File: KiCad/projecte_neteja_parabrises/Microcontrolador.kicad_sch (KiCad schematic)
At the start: 14 parts, among them J1 Conn_01x05_Pin, SW1 SW_Omron_B3FS, U3 HDC2080, Y1 Crystal

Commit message: Pines
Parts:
- renumbered C4 to C17, C5 to C3, C6 to C4, R1 to R10, R3 to R7, R2 to R9, SW1 to SW4, U3 to U6
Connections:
- net GATE B2: now reaches 11.26 (RC1)
- no-connect marks 16 -> 15
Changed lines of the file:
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@@
 	)
 	(no_connect
-		(at 34.29 73.66)
-	)
-	(no_connect
 		(at 83.82 119.38)
 	)
@@
 	(wire
 		(pts
+			(xy 30.734 73.66) (xy 34.29 73.66)
+		)
+		(stroke
+			(width 0)
+			(type default)
+		)
+	)
+	(wire
+		(pts
 			(xy 105.41 104.14) (xy 108.204 104.14)
 		)
@@
 		)
 	)
+	(global_label "GATE B2"
+		(shape input)
+		(at 30.734 73.66 180)
+		(fields_autoplaced yes)
+		(effects
+			(font
+				(size 1.27 1.27)
+			)
+			(justify right)
+		)
+		(property "Intersheetrefs" "${INTERSHEET_REFS}"
+			(at 19.8265 73.66 0)
+			(effects
+				(font
+					(size 1.27 1.27)
+				)
+				(justify right)
+				(hide yes)
+			)
+		)
+	)
 	(global_label "SCL"
 		(shape input)
@@
 		(dnp no)
 		(fields_autoplaced yes)
-		(property "Reference" "R2"
+		(property "Reference" "R9"
 			(at 254.635 26.6699 0)
 			(effects
@@
 		(dnp no)
 		(fields_autoplaced yes)
-		(property "Reference" "#PWR015"
+		(property "Reference" "#PWR037"
 			(at 34.544 38.608 0)
 			(effects
@@
 		(on_board yes)
 		(dnp no)
-		(property "Reference" "#PWR012"
+		(property "Reference" "#PWR0110"
 			(at 76.2 40.64 0)
 			(effects
@@
 		(dnp no)
 		(fields_autoplaced yes)
-		(property "Reference" "U3"
+		(property "Reference" "U6"
 			(at 236.4583 30.48 0)
 			(effects
@@
 		(on_board yes)
 		(dnp no)
-		(property "Reference" "11"
+		(property "Reference" "U?"
 			(at 68.072 87.376 0)
 			(effects
@@
 				)
 			)
+			(project "projecte_neteja_parabrises"
+				(path "/83fe8808-b70b-463e-9fcd-89556c9690a9/7b0ed2a6-dd0e-4fb8-9a3e-b81f5336277e"
+					(reference "U?")
+					(unit 1)
+				)
+			)
 		)
 	)
@@
 		(dnp no)
 		(fields_autoplaced yes)
-		(property "Reference" "C6"
+		(property "Reference" "C4"
 			(at 171.45 44.4499 0)
 			(effects
@@
 		(dnp no)
 		(fields_autoplaced yes)
-		(property "Reference" "SW1"
+		(property "Reference" "SW4"
 			(at 61.214 16.002 0)
 			(effects
@@
 		(dnp no)
 		(fields_autoplaced yes)
-		(property "Reference" "#PWR02"
+		(property "Reference" "#PWR022"
 			(at 153.035 55.88 0)
 			(effects
@@
 		(on_board yes)
 		(dnp no)
-		(property "Reference" "#PWR05"
+		(property "Reference" "#PWR?"
 			(at 81.28 39.624 0)
 			(effects
@@
 				)
 			)
+			(project "projecte_neteja_parabrises"
+				(path "/83fe8808-b70b-463e-9fcd-89556c9690a9/7b0ed2a6-dd0e-4fb8-9a3e-b81f5336277e"
+					(reference "#PWR?")
+					(unit 1)
+				)
+			)
 		)
 	)
@@
 		(dnp no)
 		(fields_autoplaced yes)
-		(property "Reference" "#PWR07"
+		(property "Reference" "#PWR036"
 			(at 70.739 29.972 0)
 			(effects
@@
 		(on_board yes)
 		(dnp no)
-		(property "Reference" "#PWR03"
+		(property "Reference" "#PWR?"
 			(at 23.622 95.758 0)
 			(effects
@@
 				)
 			)
+			(project "projecte_neteja_parabrises"
+				(path "/83fe8808-b70b-463e-9fcd-89556c9690a9/7b0ed2a6-dd0e-4fb8-9a3e-b81f5336277e"
+					(reference "#PWR?")
+					(unit 1)
+				)
+			)
 		)
 	)
@@
 		(dnp no)
 		(fields_autoplaced yes)
-		(property "Reference" "C5"
+		(property "Reference" "C3"
 			(at 156.21 44.4499 0)
 			(effects
@@
 		(on_board yes)
 		(dnp no)
-		(property "Reference" "#PWR06"
+		(property "Reference" "#PWR024"
 			(at 222.25 49.53 0)
 			(effects
@@
 		(on_board yes)
 		(dnp no)
-		(property "Reference" "C4"
+		(property "Reference" "C17"
 			(at 115.57 76.2 90)
 			(effects
@@
 		(dnp no)
 		(fields_autoplaced yes)
-		(property "Reference" "#PWR08"
+		(property "Reference" "#PWR09"
 			(at 106.68 90.17 0)
 			(effects
@@
 		(dnp no)
 		(fields_autoplaced yes)
-		(property "Reference" "#PWR014"
+		(property "Reference" "#PWR0112"
 			(at 119.888 85.09 0)
 			(effects
@@
 		(dnp no)
 		(fields_autoplaced yes)
-		(property "Reference" "#PWR04"
+		(property "Reference" "#PWR025"
 			(at 234.315 59.69 0)
 			(effects
@@
 		(on_board yes)
 		(dnp no)
-		(property "Reference" "R1"
+		(property "Reference" "R10"
 			(at 261.239 49.5301 0)
 			(effects
@@
 		(dnp no)
 		(fields_autoplaced yes)
-		(property "Reference" "#PWR01"
+		(property "Reference" "#PWR023"
 			(at 168.275 55.88 0)
 			(effects
@@
 		(on_board yes)
 		(dnp no)
-		(property "Reference" "C2"
+		(property "Reference" "C?"
 			(at 33.655 87.63 90)
 			(effects
@@
 				)
 			)
+			(project "projecte_neteja_parabrises"
+				(path "/83fe8808-b70b-463e-9fcd-89556c9690a9/7b0ed2a6-dd0e-4fb8-9a3e-b81f5336277e"
+					(reference "C?")
+					(unit 1)
+				)
+			)
 		)
 	)
@@
 		(dnp no)
 		(fields_autoplaced yes)
-		(property "Reference" "R3"
+		(property "Reference" "R7"
 			(at 52.324 17.272 90)
 			(effects

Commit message: huella
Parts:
- U4: renamed from 11; footprint (none) -> Package_DFN_QFN:QFN-44-1EP_7x7mm_P0.5mm_EP5.2x5.2mm
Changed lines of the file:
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@@
 		(on_board yes)
 		(dnp no)
-		(property "Reference" "U?"
+		(property "Reference" "U4"
 			(at 68.072 87.376 0)
 			(effects
@@
 			)
 		)
-		(property "Footprint" ""
+		(property "Footprint" "Package_DFN_QFN:QFN-44-1EP_7x7mm_P0.5mm_EP5.2x5.2mm"
 			(at 132.334 68.326 0)
 			(effects
@@
 			(project "projecte_neteja_parabrises"
 				(path "/83fe8808-b70b-463e-9fcd-89556c9690a9/7b0ed2a6-dd0e-4fb8-9a3e-b81f5336277e"
-					(reference "U?")
+					(reference "U4")
 					(unit 1)
 				)
@@
 		(on_board yes)
 		(dnp no)
-		(property "Reference" "#PWR?"
+		(property "Reference" "#PWR0101"
 			(at 81.28 39.624 0)
 			(effects
@@
 			(project "projecte_neteja_parabrises"
 				(path "/83fe8808-b70b-463e-9fcd-89556c9690a9/7b0ed2a6-dd0e-4fb8-9a3e-b81f5336277e"
-					(reference "#PWR?")
+					(reference "#PWR0101")
 					(unit 1)
 				)
@@
 		(on_board yes)
 		(dnp no)
-		(property "Reference" "#PWR?"
+		(property "Reference" "#PWR0102"
 			(at 23.622 95.758 0)
 			(effects
@@
 			(project "projecte_neteja_parabrises"
 				(path "/83fe8808-b70b-463e-9fcd-89556c9690a9/7b0ed2a6-dd0e-4fb8-9a3e-b81f5336277e"
-					(reference "#PWR?")
+					(reference "#PWR0102")
 					(unit 1)
 				)
@@
 		(on_board yes)
 		(dnp no)
-		(property "Reference" "C?"
+		(property "Reference" "C2"
 			(at 33.655 87.63 90)
 			(effects
@@
 			(project "projecte_neteja_parabrises"
 				(path "/83fe8808-b70b-463e-9fcd-89556c9690a9/7b0ed2a6-dd0e-4fb8-9a3e-b81f5336277e"
-					(reference "C?")
-					(unit 1)
-				)
+					(reference "C2")
+					(unit 1)
+				)

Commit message: pcb placement
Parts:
- Y1: footprint Crystal:Crystal_SMD_HC49-SD -> Crystal:Crystal_SMD_EuroQuartz_EQ161-2Pin_3.2x1.5mm_HandSoldering
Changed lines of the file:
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@@
 			)
 		)
-		(property "Footprint" "Crystal:Crystal_SMD_HC49-SD"
+		(property "Footprint" "Crystal:Crystal_SMD_EuroQuartz_EQ161-2Pin_3.2x1.5mm_HandSoldering"
 			(at 160.655 39.37 0)
 			(effects

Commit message: pcb
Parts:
- removed SW4: SW_Omron_B3FS, Button_Switch_SMD:SW_SPST_Omron_B3FS-100xP, symbol Switch:SW_Omron_B3FS
- added SW3: CALEFACTOR, Button_Switch_SMD:SW_Push_SPST_NO_Alps_SKRK, symbol Switch:SW_Push
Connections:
- net CANRX: now also U4.25 (RC0); no longer U4.36 (RP19)
- net CANTX: now also U4.26 (RC1); no longer U4.37 (RP20)
- net FC1: now also U4.4 (RC8); no longer U4.32 (RA8)
- net FC2: now also U4.3 (RC7); no longer U4.33 (RB4)
- net GATE B: now also U4.20 (RA1); no longer U4.25 (RC0)
- net GATE B2: now also U4.19 (RA0); no longer U4.26 (RC1)
- net GATE C: now also U4.14 (RB14); no longer U4.27 (RC2)
- net GND: now also SW3.2
- net SW1: now also U4.35 (RA9); no longer U4.2 (RC6)
- net SW2: now also U4.36 (RP19); no longer U4.3 (RC7)
- net SW3: now also U4.37 (RP20); no longer U4.4 (RC8)
- net SWB: now also U4.42 (RB6); no longer U4.20 (RA1)
- net SWC: now also U4.41 (RB5); no longer U4.19 (RA0)
- net at R7.2: now also SW3.1

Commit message: pcb
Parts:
- SW3: value CALEFACTOR -> SW
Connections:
- net GATE B2: now also U4.14 (RB14); no longer U4.19 (RA0)
- net GATE C: now also U4.13 (RA7); no longer U4.14 (RB14)
- net RX: now also U4.24 (RP3); no longer U4.23 (RP2)
- net TX: now also U4.23 (RP2); no longer U4.24 (RP3)
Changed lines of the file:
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@@
 	)
 	(no_connect
-		(at 88.9 48.26)
+		(at 59.69 45.72)
 	)
 	(no_connect
@@
 	(global_label "RX"
 		(shape input)
-		(at 29.718 58.42 180)
+		(at 29.21 63.5 180)
 		(fields_autoplaced yes)
 		(effects
@@
 		)
 		(property "Intersheetrefs" "${INTERSHEET_REFS}"
-			(at 24.2533 58.42 0)
+			(at 23.7453 63.5 0)
 			(effects
 				(font
@@
 	(global_label "GATE C"
 		(shape input)
-		(at 83.82 48.26 90)
-		(fields_autoplaced yes)
-		(effects
-			(font
-				(size 1.27 1.27)
-			)
-			(justify left)
-		)
-		(property "Intersheetrefs" "${INTERSHEET_REFS}"
-			(at 83.82 38.562 90)
+		(at 88.9 48.26 90)
+		(fields_autoplaced yes)
+		(effects
+			(font
+				(size 1.27 1.27)
+			)
+			(justify left)
+		)
+		(property "Intersheetrefs" "${INTERSHEET_REFS}"
+			(at 88.9 38.562 90)
 			(effects
 				(font
@@
 	(global_label "GATE B2"
 		(shape input)
-		(at 59.69 45.72 90)
-		(fields_autoplaced yes)
-		(effects
-			(font
-				(size 1.27 1.27)
-			)
-			(justify left)
-		)
-		(property "Intersheetrefs" "${INTERSHEET_REFS}"
-			(at 59.69 34.8125 90)
+		(at 83.82 48.26 90)
+		(fields_autoplaced yes)
+		(effects
+			(font
+				(size 1.27 1.27)
+			)
+			(justify left)
+		)
+		(property "Intersheetrefs" "${INTERSHEET_REFS}"
+			(at 83.82 37.3525 90)
 			(effects
 				(font
@@
 	(global_label "TX"
 		(shape output)
-		(at 29.21 63.5 180)
+		(at 29.718 58.42 180)
 		(fields_autoplaced yes)
 		(effects
@@
 		)
 		(property "Intersheetrefs" "${INTERSHEET_REFS}"
-			(at 24.0477 63.5 0)
+			(at 24.5557 58.42 0)
 			(effects
 				(font
@@
 			)
 		)
-		(property "Value" "CALEFACTOR"
+		(property "Value" "SW"
 			(at 63.119 17.907 0)
 			(effects

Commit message: pcb
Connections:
- net FC1: now also U4.34 (RA4); no longer U4.4 (RC8)
- net FC2: now also U4.33 (RB4); no longer U4.3 (RC7)
- net SW1: now also U4.11 (RB13); no longer U4.35 (RA9)
- net SW2: now also U4.4 (RC8); no longer U4.36 (RP19)
- net SW3: now also U4.3 (RC7); no longer U4.37 (RP20)
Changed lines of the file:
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@@
+	)
+	(no_connect
+		(at 105.41 88.9)
 	)
 	(no_connect
@@
 	)
 	(no_connect
-		(at 31.242 109.22)
+		(at 48.26 119.38)
 	)
 	(no_connect
@@
 	)
 	(no_connect
-		(at 105.41 88.9)
+		(at 58.42 119.38)
 	)
 	(no_connect
-		(at 44.45 119.38)
-	)
-	(no_connect
-		(at 105.41 58.42)
+		(at 53.34 124.46)
 	)
 	(no_connect
@@
 	(wire
 		(pts
-			(xy 58.42 119.38) (xy 58.42 124.46)
-		)
-		(stroke
-			(width 0)
-			(type default)
-		)
-	)
-	(wire
-		(pts
 			(xy 39.37 27.432) (xy 39.37 28.702)
 		)
@@
 	(wire
 		(pts
-			(xy 31.242 109.22) (xy 34.29 109.22)
-		)
-		(stroke
-			(width 0)
-			(type default)
-		)
-	)
-	(wire
-		(pts
 			(xy 29.718 58.42) (xy 34.29 58.42)
 		)
@@
 	(global_label "FC1"
 		(shape input)
-		(at 109.22 93.98 0)
-		(fields_autoplaced yes)
-		(effects
-			(font
-				(size 1.27 1.27)
-			)
-			(justify left)
-		)
-		(property "Intersheetrefs" "${INTERSHEET_REFS}"
-			(at 115.7733 93.98 0)
-			(effects
-				(font
-					(size 1.27 1.27)
-				)
-				(justify left)
+		(at 44.45 119.38 270)
+		(fields_autoplaced yes)
+		(effects
+			(font
+				(size 1.27 1.27)
+			)
+			(justify right)
+		)
+		(property "Intersheetrefs" "${INTERSHEET_REFS}"
+			(at 44.45 125.9333 90)
+			(effects
+				(font
+					(size 1.27 1.27)
+				)
+				(justify right)
 				(hide yes)
 			)
@@
 	(global_label "SW3"
 		(shape input)
-		(at 58.42 124.46 270)
-		(fields_autoplaced yes)
-		(effects
-			(font
-				(size 1.27 1.27)
-			)
-			(justify right)
-		)
-		(property "Intersheetrefs" "${INTERSHEET_REFS}"
-			(at 58.42 131.3156 90)
-			(effects
-				(font
-					(size 1.27 1.27)
-				)
-				(justify right)
+		(at 108.458 99.06 0)
+		(fields_autoplaced yes)
+		(effects
+			(font
+				(size 1.27 1.27)
+			)
+			(justify left)
+		)
+		(property "Intersheetrefs" "${INTERSHEET_REFS}"
+			(at 115.3136 99.06 0)
+			(effects
+				(font
+					(size 1.27 1.27)
+				)
+				(justify left)
 				(hide yes)
 			)
@@
 	(global_label "SW1"
 		(shape input)
-		(at 48.26 119.38 270)
-		(fields_autoplaced yes)
-		(effects
-			(font
-				(size 1.27 1.27)
-			)
-			(justify right)
-		)
-		(property "Intersheetrefs" "${INTERSHEET_REFS}"
-			(at 48.26 126.2356 90)
-			(effects
-				(font
-					(size 1.27 1.27)
-				)
-				(justify right)
+		(at 105.41 58.42 0)
+		(fields_autoplaced yes)
+		(effects
+			(font
+				(size 1.27 1.27)
+			)
+			(justify left)
+		)
+		(property "Intersheetrefs" "${INTERSHEET_REFS}"
+			(at 112.2656 58.42 0)
+			(effects
+				(font
+					(size 1.27 1.27)
+				)
+				(justify left)
 				(hide yes)
 			)
@@
 	(global_label "FC2"
 		(shape input)
-		(at 108.458 99.06 0)
-		(fields_autoplaced yes)
-		(effects
-			(font
-				(size 1.27 1.27)
-			)
-			(justify left)
-		)
-		(property "Intersheetrefs" "${INTERSHEET_REFS}"
-			(at 115.0113 99.06 0)
-			(effects
-				(font
-					(size 1.27 1.27)
-				)
-				(justify left)
+		(at 34.29 109.22 180)
+		(fields_autoplaced yes)
+		(effects
+			(font
+				(size 1.27 1.27)
+			)
+			(justify right)
+		)
+		(property "Intersheetrefs" "${INTERSHEET_REFS}"
+			(at 27.7367 109.22 0)
+			(effects
+				(font
+					(size 1.27 1.27)
+				)
+				(justify right)
 				(hide yes)
 			)
@@
 	(global_label "SW2"
 		(shape input)
-		(at 53.34 124.46 270)
-		(fields_autoplaced yes)
-		(effects
-			(font
-				(size 1.27 1.27)
-			)
-			(justify right)
-		)
-		(property "Intersheetrefs" "${INTERSHEET_REFS}"
-			(at 53.34 131.3156 90)
-			(effects
-				(font
-					(size 1.27 1.27)
-				)
-				(justify right)
-				(hide yes)
-			)
+		(at 109.22 93.98 0)
+		(fields_autoplaced yes)
+		(effects
+			(font
+				(size 1.27 1.27)
+			)
+			(justify left)
+		)
+		(property "Intersheetrefs" "${INTERSHEET_REFS}"
+			(at 116.0756 93.98 0)
+			(effects
+				(font
+					(size 1.27 1.27)
+				)
+				(justify left)
+				(hide yes)
+			)

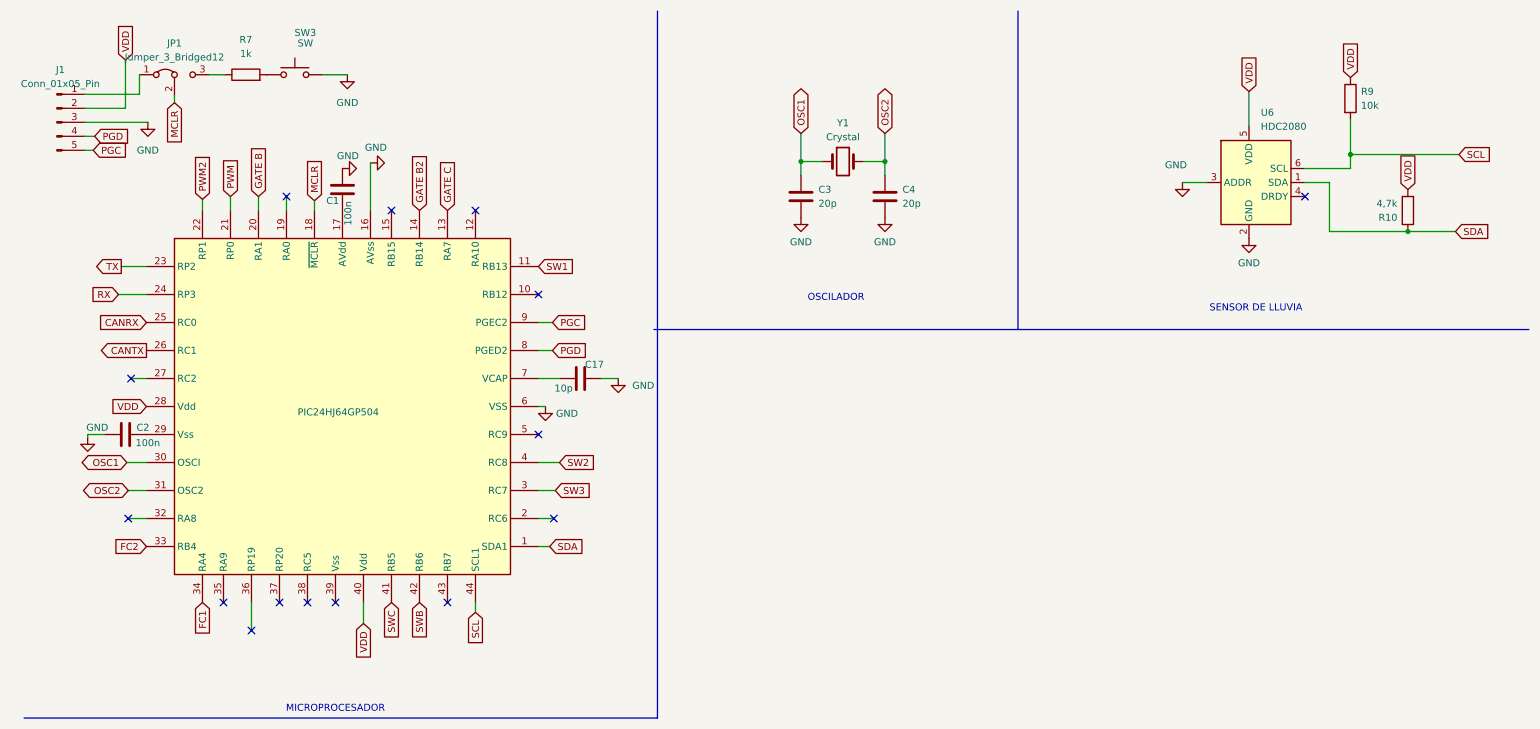
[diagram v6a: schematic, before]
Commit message: actualitzacio pcb
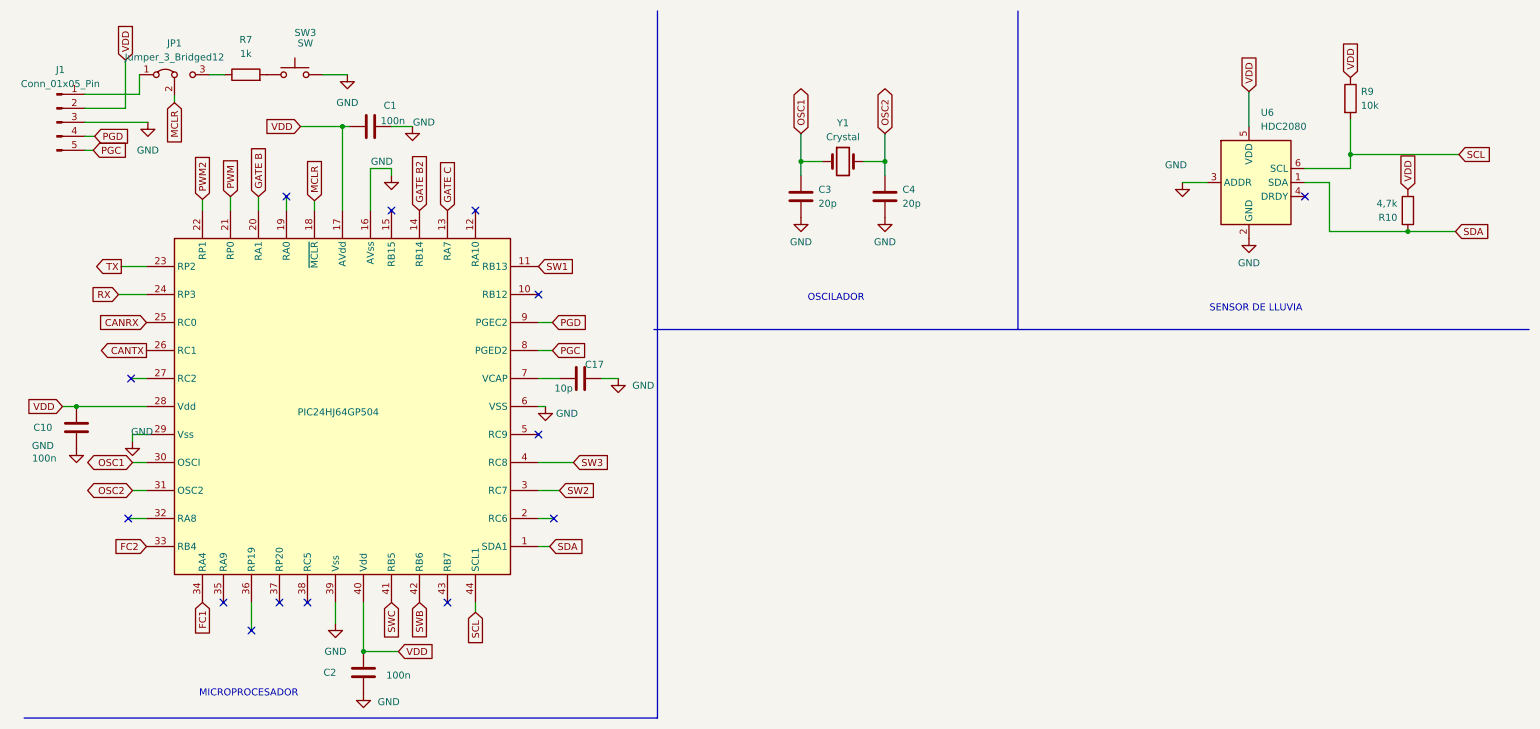
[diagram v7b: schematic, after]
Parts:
- added C10: 100n, Capacitor_SMD:C_0805_2012Metric, symbol Device:C
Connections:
- net GND: now also C1.1, U4.29 (Vss), U4.39 (Vss), C10.1; no longer C1.2
- net PGC: now also U4.8 (PGED2); no longer U4.9 (PGEC2)
- net PGD: now also U4.9 (PGEC2); no longer U4.8 (PGED2)
- net SW2: now also U4.3 (RC7); no longer U4.4 (RC8)
- net SW3: now also U4.4 (RC8); no longer U4.3 (RC7)
- net VDD: now also C1.2, C2.2, U4.17 (AVdd), C10.2
- no-connect marks 15 -> 14
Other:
- moved on the sheet: C1

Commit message: vias pcb
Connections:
- net VDD: no longer U6.5 (VDD)
- new net 5V: U6.5 (VDD)
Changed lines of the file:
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@@
 		)
 	)
-	(global_label "VDD"
+	(global_label "5V"
 		(shape input)
 		(at 234.315 26.67 90)
@@
 		)
 		(property "Intersheetrefs" "${INTERSHEET_REFS}"
-			(at 234.315 20.0562 90)
+			(at 234.315 21.3867 90)
 			(effects
 				(font
